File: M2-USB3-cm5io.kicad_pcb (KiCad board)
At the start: 4 copper layers, 23.7 x 80.1 mm, 52 parts, among them J1 Bus_M.2_Socket_M, J2 Conn_01x16_MountingPin, J3 Conn_01x16_MountingPin, J4 USB3_A, U1 VL805, U18 MP3422GG-P, U2 W25Q32JVZP, U4 TLV62568ADRLR, Y1 25Mhz

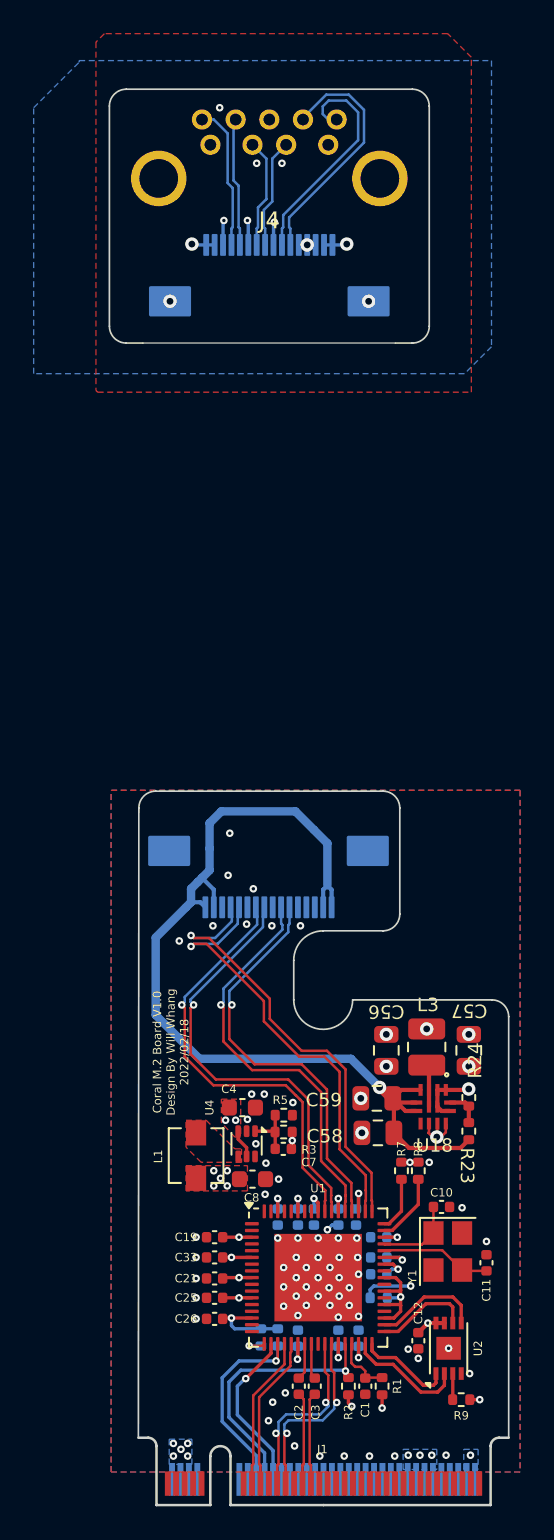
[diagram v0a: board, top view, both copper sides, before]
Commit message: Fix most ERC/DRC errors
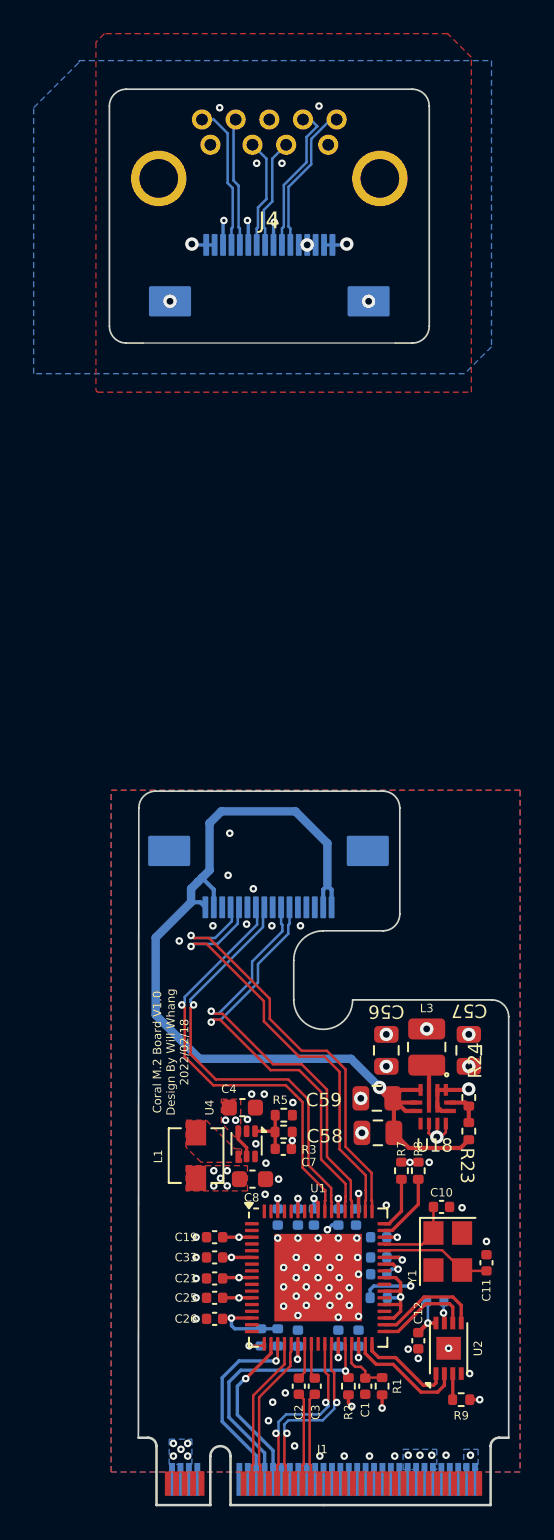
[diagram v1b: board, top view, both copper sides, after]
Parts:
- added R10: 10K, Resistor_SMD:R_0402_1005Metric, B.Cu at (118.8, 117.4)
- J1: footprint NGFF:NGFF_M -> footprints:NGFF_M
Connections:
- J1 pad 10: PCIe_LED -> unconnected-(J1-DAS/~{DSS}/~{LED1}-Pad10)
- J2 pad 10: USB3_RX1- -> USB3_RX1+
- J2 pad 11: USB3_RX1+ -> USB3_RX1-
- J3 pad 6: USB3_RX1+ -> USB3_RX1-
- J3 pad 7: USB3_RX1- -> USB3_RX1+
- U2 pad 7: +3.3VA -> Net-(U2-IO3)
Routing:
- net USB3_RX1+: track 38.9 -> 34.0 mm
- net USB3_RX1-: track 38.0 -> 34.0 mm
- net Net-(U2-IO3): track 0.00 -> 1.33 mm, vias 0 -> 1
- net +3.3VA: track 28.0 -> 28.8 mm
- net GND: vias 83 -> 85
